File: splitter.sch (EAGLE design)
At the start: 14 parts

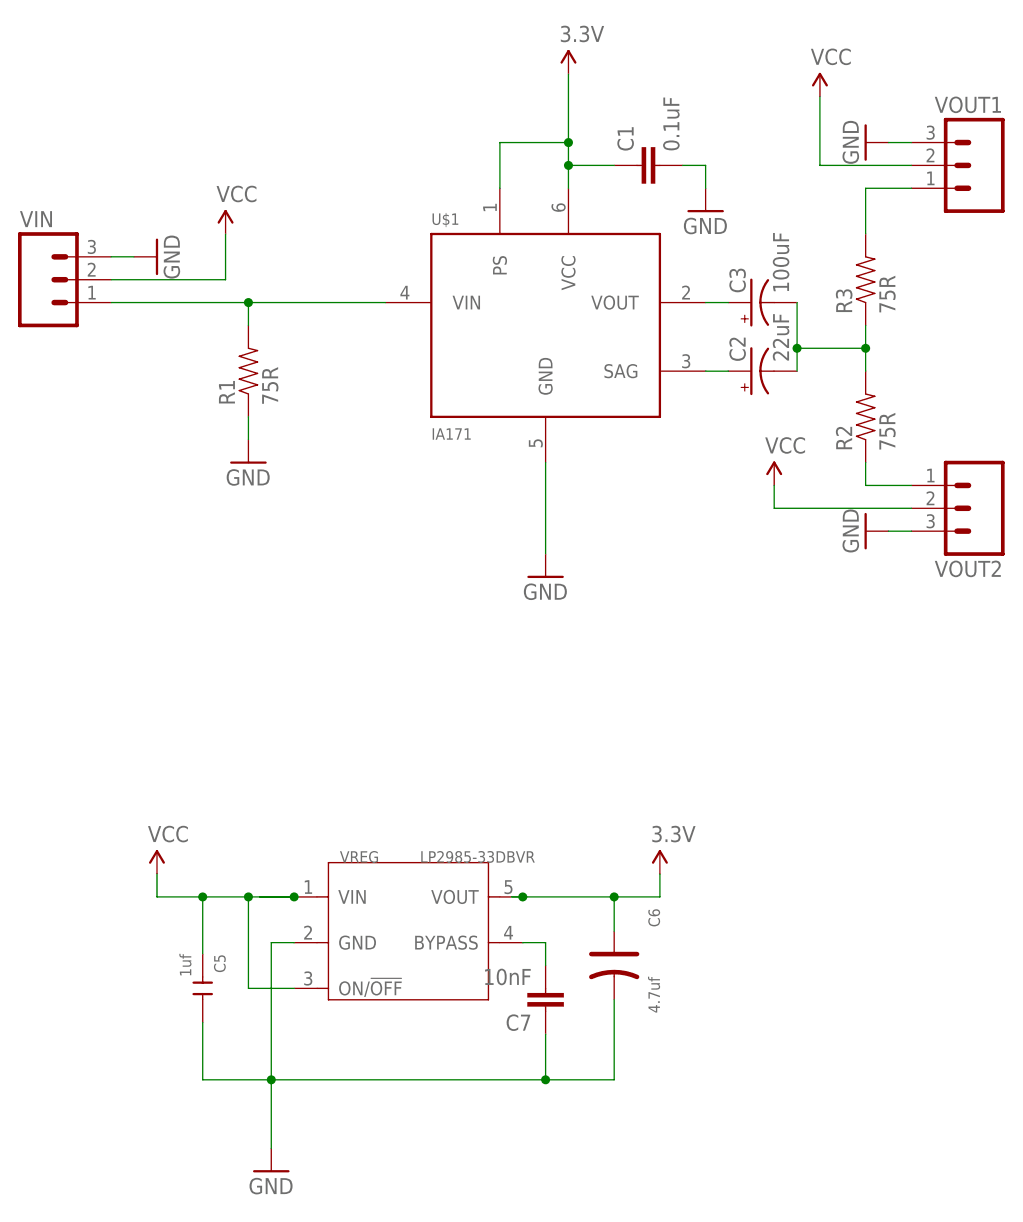
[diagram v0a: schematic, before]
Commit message: Standardized the capacitors and increased their values for VREG IN/OUT
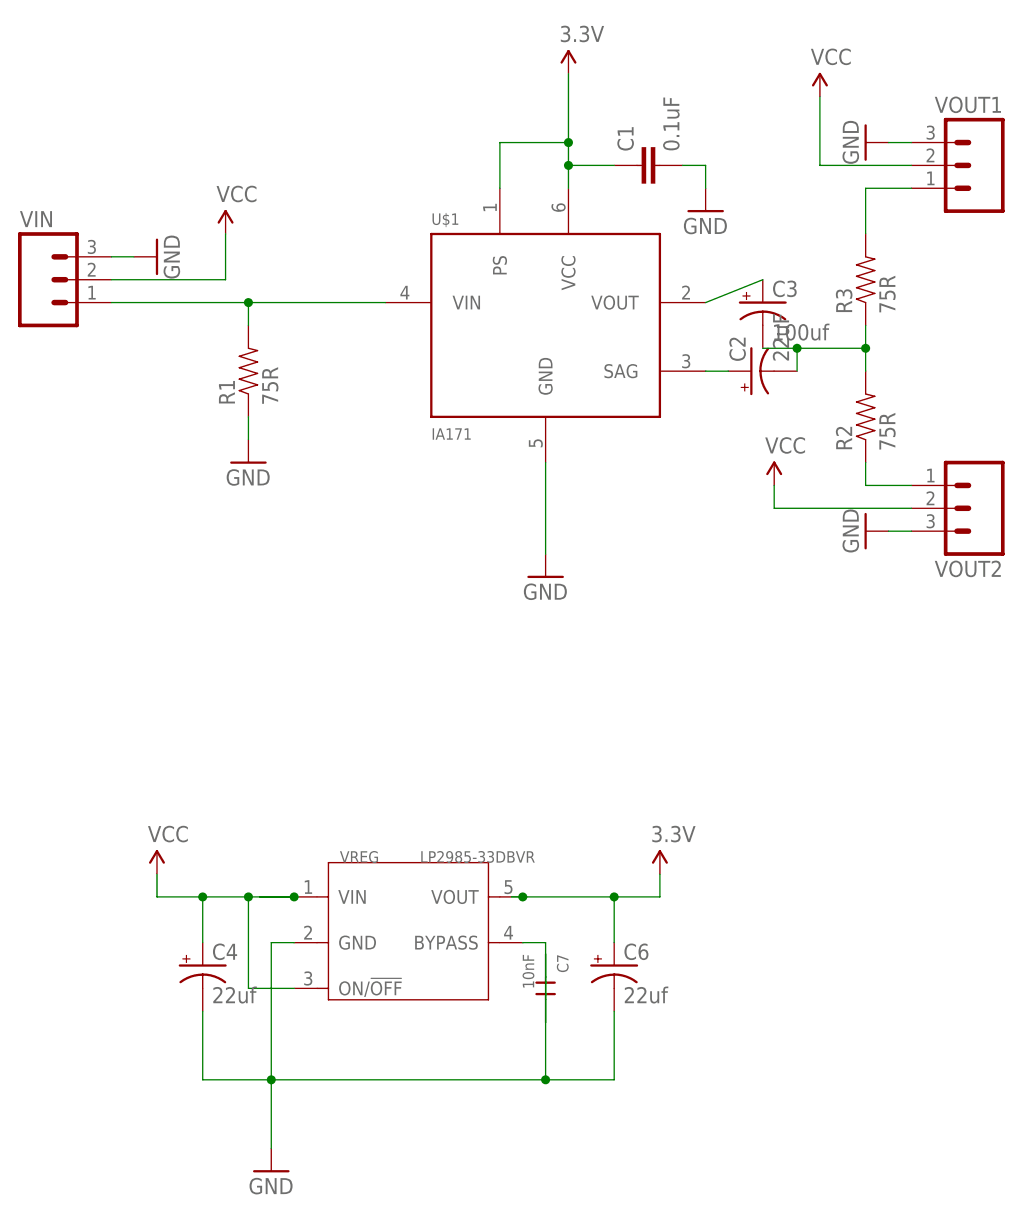
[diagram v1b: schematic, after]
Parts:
- removed C5: 1uf, Seeed-OPL-Capacitor:CERAMIC-1UF-25V-10%-X7R(0603)
- added C4: 22uf, SparkFun-Passives:CAP_POL1206
- C3: value 100uF -> 100uf; device SparkFun-Passives:CAP_POL1206 -> SparkFun-Passives:CAP_POL3528
- C6: value 4.7uf -> 22uf; device Seeed-OPL-Capacitor:TANTALUM-SMD-4.7UF-16V(AVX-A) -> SparkFun-Passives:CAP_POL1206
- C7: device SparkFun-Passives:CAP0805 -> Seeed-OPL-Capacitor:CERAMIC-10NF-50V-5%-X7R(0805)
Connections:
- net GND: now also C4.-; no longer C5.2
- net VCC: now also C4.+; no longer C5.1
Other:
- moved on the sheet: C3
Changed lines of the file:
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@@
 <part name="C2" library="SparkFun-Passives" deviceset="CAP_POL" device="1206" value="22uF"/>
 <part name="R1" library="SparkFun-Passives" deviceset="RESISTOR" device="0805-RES" value="75R"/>
-<part name="C3" library="SparkFun-Passives" deviceset="CAP_POL" device="1206" value="100uF"/>
+<part name="C3" library="SparkFun-Passives" deviceset="CAP_POL" device="3528" value="100uf"/>
 <part name="R2" library="SparkFun-Passives" deviceset="RESISTOR" device="0805-RES" value="75R"/>
 <part name="R3" library="SparkFun-Passives" deviceset="RESISTOR" device="0805-RES" value="75R"/>
@@
 <part name="SUPPLY6" library="SparkFun-Aesthetics" deviceset="3.3V" device=""/>
 <part name="GND7" library="SparkFun-Aesthetics" deviceset="GND" device=""/>
-<part name="C5" library="Seeed-OPL-Capacitor" deviceset="CERAMIC-1UF-25V-10%-X7R(0603)" device="" value="1uf"/>
-<part name="C6" library="Seeed-OPL-Capacitor" deviceset="TANTALUM-SMD-4.7UF-16V(AVX-A)" device="" value="4.7uf"/>
+<part name="C6" library="SparkFun-Passives" deviceset="CAP_POL" device="1206" value="22uf"/>
 <part name="VREG" library="Seeed-OPL-ic" deviceset="PMIC-LP2985-33DBVR(SOT23-5)" device="" value="LP2985-33DBVR"/>
-<part name="C7" library="SparkFun-Passives" deviceset="CAP" device="0805" value="10nF"/>
+<part name="C7" library="Seeed-OPL-Capacitor" deviceset="CERAMIC-10NF-50V-5%-X7R(0805)" device="" value="10nF"/>
+<part name="C4" library="SparkFun-Passives" deviceset="CAP_POL" device="1206" value="22uf"/>
 </parts>
 <sheets>
@@
 <instance part="C2" gate="G$1" x="99.06" y="83.82" rot="R90"/>
 <instance part="R1" gate="G$1" x="43.18" y="83.82" rot="R90"/>
-<instance part="C3" gate="G$1" x="99.06" y="91.44" rot="R90"/>
+<instance part="C3" gate="G$1" x="100.33" y="91.44"/>
 <instance part="R2" gate="G$1" x="111.76" y="78.74" rot="R90"/>
 <instance part="R3" gate="G$1" x="111.76" y="93.98" rot="R90"/>
@@
 <instance part="SUPPLY6" gate="G$1" x="88.9" y="27.94"/>
 <instance part="GND7" gate="1" x="45.72" y="-5.08"/>
-<instance part="C5" gate="G$1" x="38.1" y="15.24" rot="R270"/>
-<instance part="C6" gate="G$1" x="83.82" y="17.78" rot="R270"/>
+<instance part="C6" gate="G$1" x="83.82" y="17.78"/>
 <instance part="VREG" gate="G$1" x="60.96" y="20.32"/>
-<instance part="C7" gate="G$1" x="76.2" y="15.24" rot="R180"/>
+<instance part="C7" gate="G$1" x="76.2" y="15.24" rot="R270"/>
+<instance part="C4" gate="G$1" x="38.1" y="17.78"/>
 </instances>
 <busses>
@@
 <wire x1="88.9" y1="25.4" x2="88.9" y2="27.94" width="0.1524" layer="91"/>
 <pinref part="C6" gate="G$1" pin="+"/>
-<wire x1="83.82" y1="25.4" x2="83.82" y2="21.59" width="0.1524" layer="91"/>
+<wire x1="83.82" y1="25.4" x2="83.82" y2="20.32" width="0.1524" layer="91"/>
 <wire x1="72.39" y1="25.4" x2="73.66" y2="25.4" width="0.1524" layer="91"/>
 <junction x="83.82" y="25.4"/>
@@
 <pinref part="U$1" gate="G$1" pin="VOUT"/>
 <pinref part="C3" gate="G$1" pin="+"/>
-<wire x1="93.98" y1="91.44" x2="96.52" y2="91.44" width="0.1524" layer="91"/>
+<wire x1="93.98" y1="91.44" x2="100.33" y2="93.98" width="0.1524" layer="91"/>
 </segment>
 </net>
@@
 <pinref part="R2" gate="G$1" pin="2"/>
 <pinref part="R3" gate="G$1" pin="1"/>
-<wire x1="104.14" y1="86.36" x2="104.14" y2="91.44" width="0.1524" layer="91"/>
+<wire x1="104.14" y1="86.36" x2="100.33" y2="86.36" width="0.1524" layer="91"/>
 <wire x1="111.76" y1="83.82" x2="111.76" y2="86.36" width="0.1524" layer="91"/>
 <wire x1="111.76" y1="86.36" x2="111.76" y2="88.9" width="0.1524" layer="91"/>
@@
 <pinref part="GND7" gate="1" pin="GND"/>
 <wire x1="45.72" y1="20.32" x2="45.72" y2="5.08" width="0.1524" layer="91"/>
-<pinref part="C5" gate="G$1" pin="2"/>
 <wire x1="45.72" y1="5.08" x2="45.72" y2="-2.54" width="0.1524" layer="91"/>
 <wire x1="45.72" y1="5.08" x2="38.1" y2="5.08" width="0.1524" layer="91"/>
-<wire x1="38.1" y1="5.08" x2="38.1" y2="11.43" width="0.1524" layer="91"/>
+<wire x1="38.1" y1="5.08" x2="38.1" y2="12.7" width="0.1524" layer="91"/>
 <junction x="45.72" y="5.08"/>
 <pinref part="C6" gate="G$1" pin="-"/>
 <wire x1="45.72" y1="5.08" x2="76.2" y2="5.08" width="0.1524" layer="91"/>
 <wire x1="76.2" y1="5.08" x2="83.82" y2="5.08" width="0.1524" layer="91"/>
-<wire x1="83.82" y1="5.08" x2="83.82" y2="13.97" width="0.1524" layer="91"/>
+<wire x1="83.82" y1="5.08" x2="83.82" y2="12.7" width="0.1524" layer="91"/>
 <pinref part="VREG" gate="G$1" pin="GND"/>
 <wire x1="45.72" y1="20.32" x2="48.26" y2="20.32" width="0.1524" layer="91"/>
 <pinref part="C7" gate="G$1" pin="1"/>
-<wire x1="76.2" y1="5.08" x2="76.2" y2="10.16" width="0.1524" layer="91"/>
+<wire x1="76.2" y1="5.08" x2="76.2" y2="19.05" width="0.1524" layer="91"/>
 <junction x="76.2" y="5.08"/>
+<pinref part="C4" gate="G$1" pin="-"/>
 </segment>
 </net>
@@
 <wire x1="38.1" y1="25.4" x2="33.02" y2="25.4" width="0.1524" layer="91"/>
 <wire x1="33.02" y1="25.4" x2="33.02" y2="27.94" width="0.1524" layer="91"/>
-<pinref part="C5" gate="G$1" pin="1"/>
-<wire x1="38.1" y1="25.4" x2="38.1" y2="19.05" width="0.1524" layer="91"/>
+<wire x1="38.1" y1="25.4" x2="38.1" y2="20.32" width="0.1524" layer="91"/>
 <wire x1="44.45" y1="25.4" x2="48.26" y2="25.4" width="0.1524" layer="91"/>
 <junction x="38.1" y="25.4"/>
@@
 <wire x1="43.18" y1="15.24" x2="43.18" y2="25.4" width="0.1524" layer="91"/>
 <junction x="43.18" y="25.4"/>
+<pinref part="C4" gate="G$1" pin="+"/>
 </segment>
 </net>
@@
 <pinref part="C7" gate="G$1" pin="2"/>
 <wire x1="73.66" y1="20.32" x2="76.2" y2="20.32" width="0.1524" layer="91"/>
-<wire x1="76.2" y1="20.32" x2="76.2" y2="17.78" width="0.1524" layer="91"/>
-</segment>
-</net>
+<wire x1="76.2" y1="20.32" x2="76.2" y2="11.43" width="0.1524" layer="91"/>
+</segment>
+</net>
